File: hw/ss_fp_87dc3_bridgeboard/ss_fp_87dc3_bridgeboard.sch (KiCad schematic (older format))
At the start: 16 parts, among them J101 Conn_01x02, J102 Conn_01x04, J103 Conn_01x03, J104 Conn_01x02, J105 Conn_01x04, J106 Conn_01x03, J107 Conn_01x02, J108 Conn_01x04, J109 Conn_01x02, J110 Conn_01x04, J111 Conn_01x03, J112 Conn_01x03

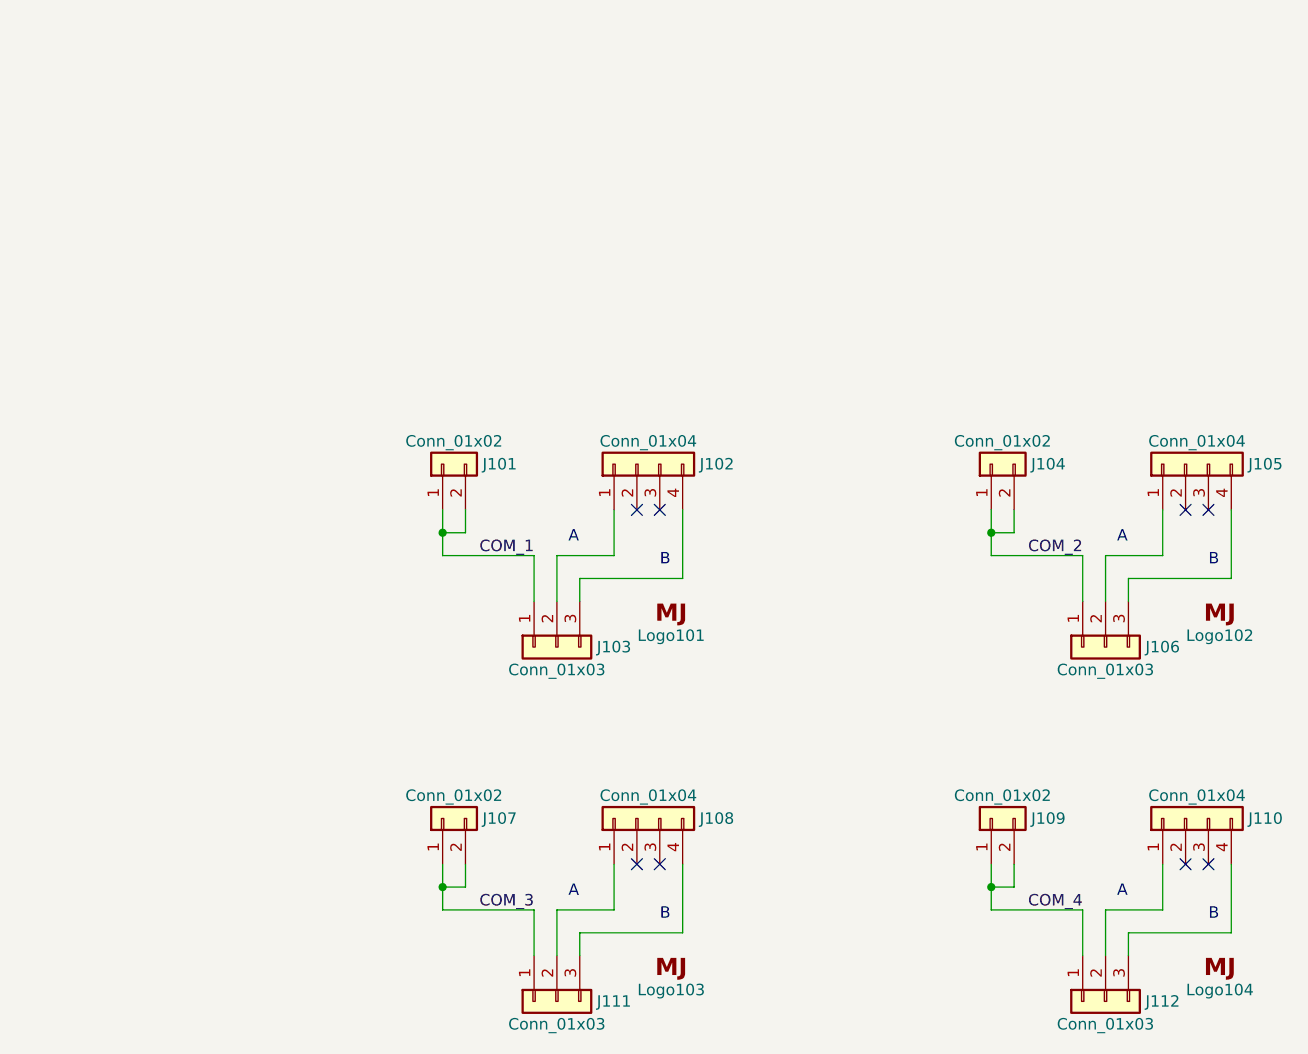
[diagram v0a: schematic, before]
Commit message: Adjust separate bridge-board panel for potential production (R1A *not* ordered though)
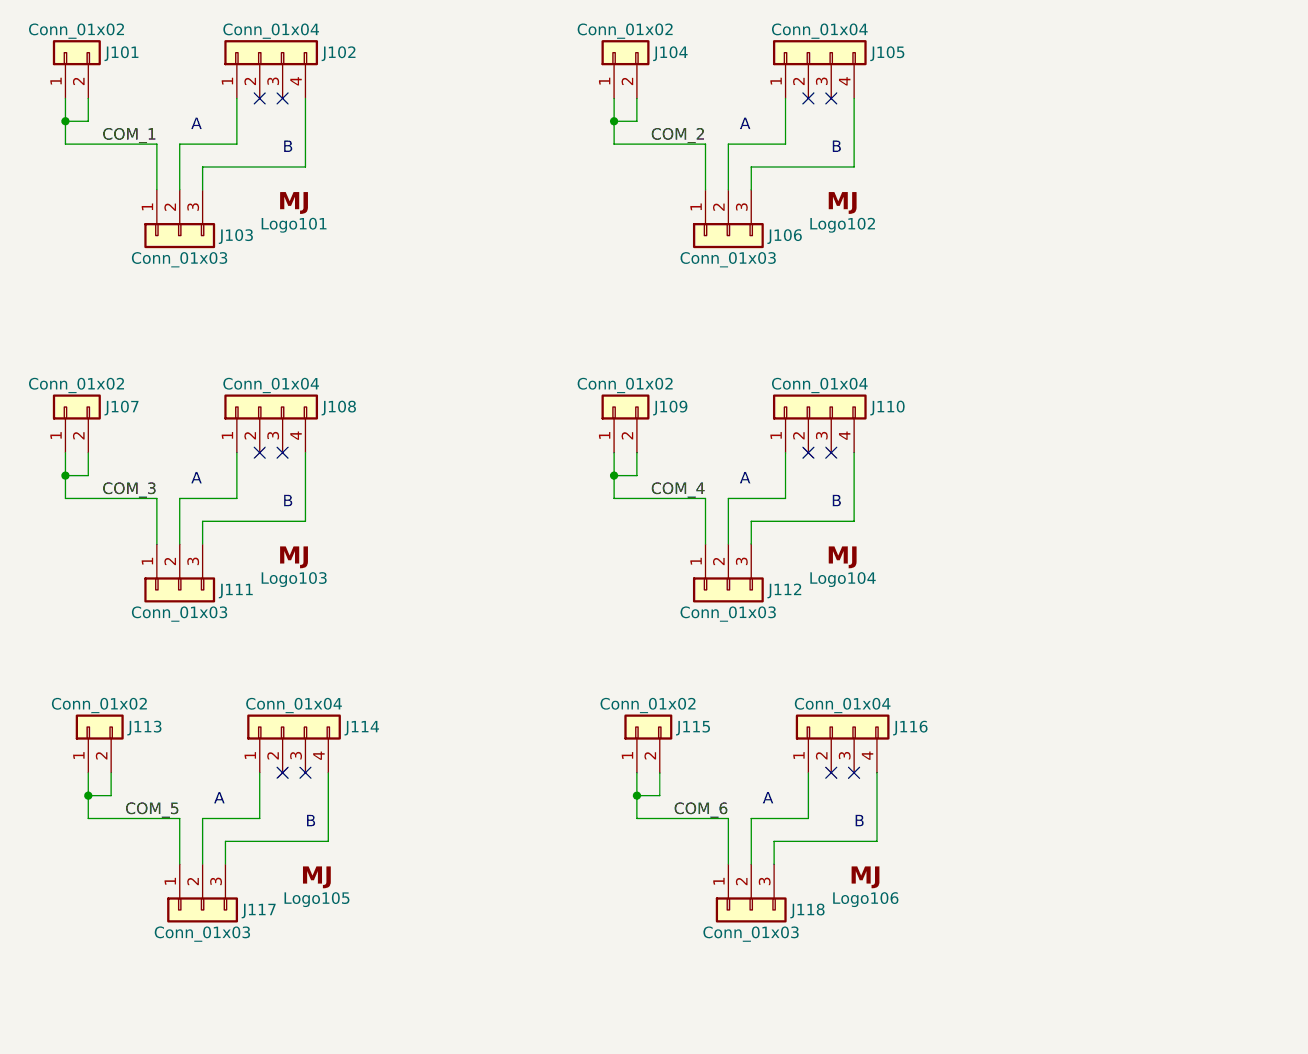
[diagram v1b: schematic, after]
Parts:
- added J113, J115: Conn_01x02, Connector_PinSocket_2.54mm:PinSocket_1x02_P2.54mm_Vertical, symbol Connector_Generic:Conn_01x02
- added J114, J116: Conn_01x04, Connector_PinSocket_2.54mm:PinSocket_1x04_P2.54mm_Vertical, symbol Connector_Generic:Conn_01x04
- added J117, J118: Conn_01x03, Connector_PinSocket_2.54mm:PinSocket_1x03_P2.54mm_Vertical, symbol Connector_Generic:Conn_01x03
- added Logo105, Logo106: Logo_MJ, customlib_mj_fp:MJ_Mini, symbol customlib_mj:Logo_MJ
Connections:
- new net: J114.1 (Pin_1), J117.2 (Pin_2)
- new net: J114.4 (Pin_4), J117.3 (Pin_3)
- new net: J116.1 (Pin_1), J118.2 (Pin_2)
- new net: J116.4 (Pin_4), J118.3 (Pin_3)
- new net COM_5: J113.1 (Pin_1), J113.2 (Pin_2), J117.1 (Pin_1)
- new net COM_6: J115.1 (Pin_1), J115.2 (Pin_2), J118.1 (Pin_1)
- no-connect marks 8 -> 12
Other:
- moved on the sheet: J101, J102, J103, J104, J105, J106, J107, J108, J109, J110, J111, J112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
